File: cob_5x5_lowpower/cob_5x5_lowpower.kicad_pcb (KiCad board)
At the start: 2 copper layers, 30 x 30 mm, 19 parts, among them J1 Conn_01x03, J2 Conn_01x03, Q1 Q_PMOS_GSD, Q2 Q_PMOS_GSD, Q3 Q_PMOS_GSD, U1 WS2811

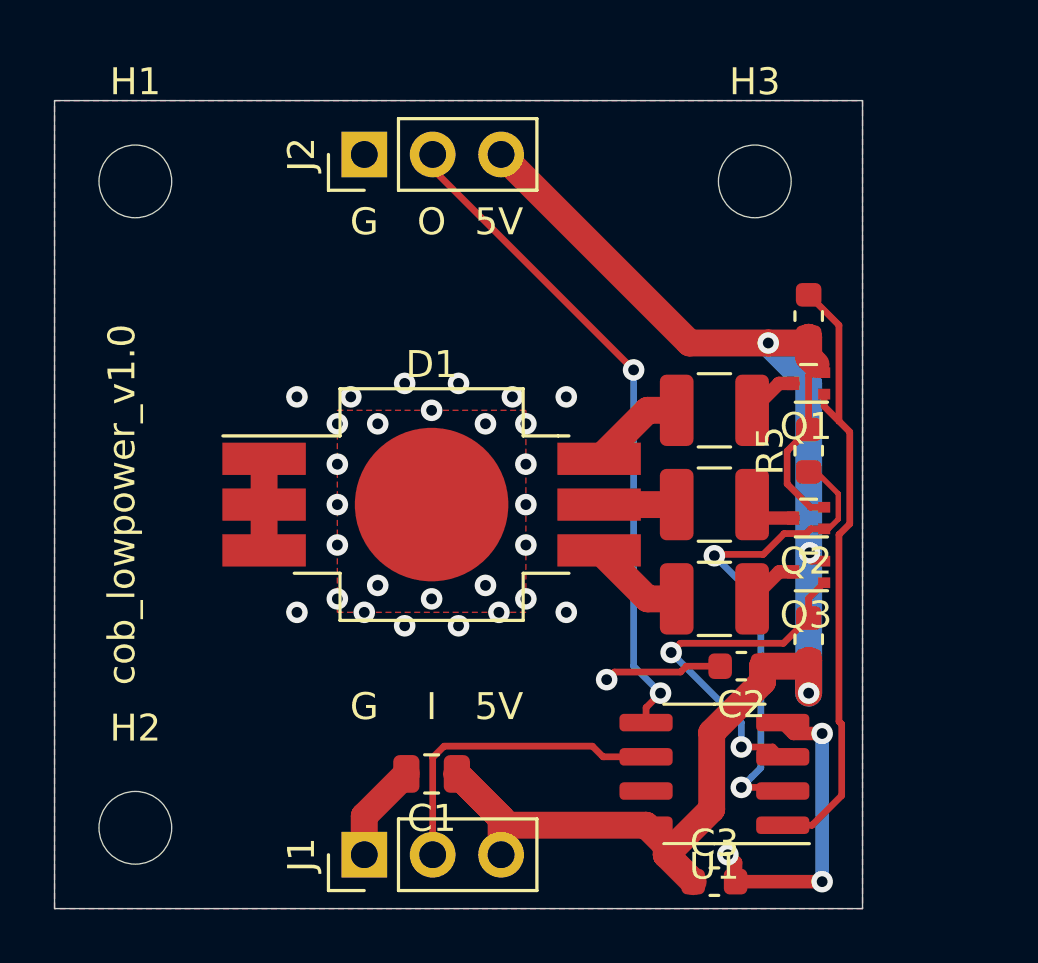
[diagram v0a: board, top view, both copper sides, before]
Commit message: Lowpower one-off revision 1.0.
Updated previous attempt (unfabricated) with lessons from from
high-power board.
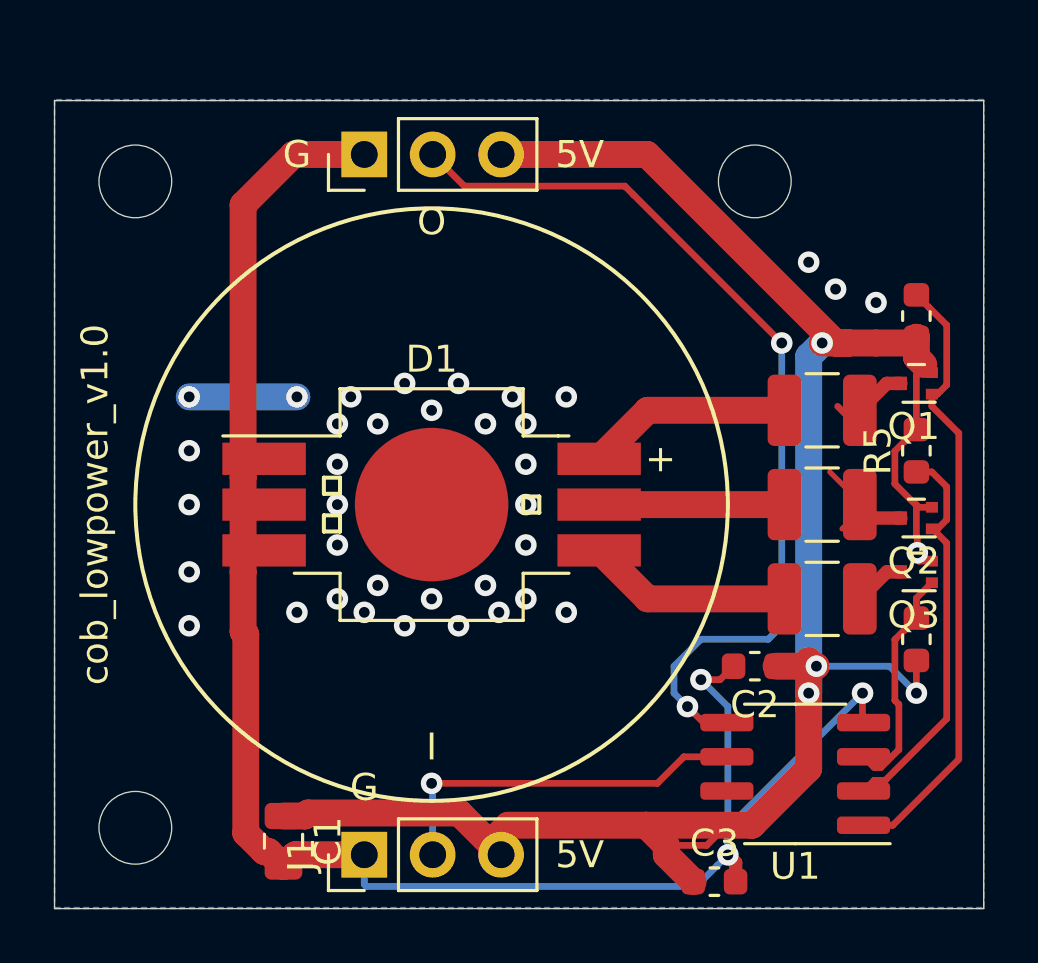
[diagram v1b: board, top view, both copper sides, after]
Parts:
- D1: value LED_RGB -> LED_RGB_EP; footprint LED_SMD:LED_RGB_Getian_GT-P6PRGB4303 -> homebrew:LED_RGB_EPISTAR_6PIN_RGB
- moved C1 6.04 mm to (109.5, 127.5), turned to 270 degrees
- moved Q1 4.00 mm to (133.0, 110.5)
- moved Q2 4.00 mm to (133.0, 115.5)
- moved Q3 4.00 mm to (133.0, 117.5)
- moved R1 4.00 mm to (129.5, 111.5)
- moved R2 4.00 mm to (129.5, 115.0)
- moved R3 4.00 mm to (129.5, 118.5)
- moved R4 4.00 mm to (133.0, 108.0)
- moved R5 4.00 mm to (133.0, 113.0)
- moved R6 4.00 mm to (133.0, 120.0)
- moved U1 3.00 mm to (128.5, 125.0)
- moved C2 0.50 mm to (127.0, 121.0)
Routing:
- net GND: track 25.2 -> 71.6 mm, vias 32 -> 3
- net +5V: track 62.5 -> 82.0 mm, vias 3 -> 5
- net DOUT: track 24.8 -> 34.4 mm
- net B_INV: track 13.5 -> 8.58 mm, vias 2 -> 0
- net R_LED: track 3.63 -> 7.63 mm
- net Net-(D1-Pad7): track 0.00 -> 4.00 mm, vias 0 -> 36
- net G_LED: track 2.88 -> 6.88 mm
- net B_LED: track 3.63 -> 7.63 mm
- net G_INV: track 18.8 -> 15.2 mm, vias 2 -> 0
- net Net-(Q2-Pad3): track 1.73 -> 4.90 mm
- net DIN: track 11.9 -> 14.0 mm, vias 0 -> 1
- net Net-(Q1-Pad3): track 1.94 -> 2.72 mm
- added copper zone on B.Cu, net Net-(D1-Pad7)
- added copper zone on F.Cu, net Net-(D1-Pad7)
- removed copper zone on B.Cu, net GND
- removed copper zone on F.Cu, net GND
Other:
- board size 30 x 30 mm -> 34.5 x 30 mm
